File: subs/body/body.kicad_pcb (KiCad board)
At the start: 2 copper layers, 40.8 x 54.8 mm, 80 parts, among them IC1 ATMEGA328P(B), P1 CON_BAT_IN, P3 CON_POLOLU_PWR2, P4 CONN_BREAKOUT4, P5 CONN_BREAKOUT2, P6 CONN_BREAKOUT3, P7 CONN_BREAKOUT5, P8 CON_BAT_OUT, Q1 CSD25402Q3A, Q2 CSD25402Q3A, Q3 CSD25402Q3A, Q4 CSD25402Q3A, Q5 CSD25402Q3A, Q6 CSD25402Q3A, SW1 SPST_Small, SW2 SPST_Small, U1 LTC4412, U10 74LVC2G07, U11 74LVC2G07, U12 LTC4412, U2 LTC4412, U3 DRV8834-SSOP, U4 TMP36GRT, U5 LTC4412, U6 RT9715GGB, 0.7A, U7 RT9715GGB, 0.7A, U8 RT9715GGB, 0.7A, U9 RT9715GGB, 0.7A, Y1 16MHz

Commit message: Before major layout change
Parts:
- removed C13: 100nF, Capacitors_SMD:C_0402
- removed U4: TMP36GRT, TO_SOT_Packages_SMD:SOT-23-5_Handsoldering
- P4: value CONN_BREAKOUT4 -> CONN3
- P5: value CONN_BREAKOUT2 -> CONN1; footprint Socket_Strips:Socket_Strip_Straight_1x12_Pitch1.27mm -> Socket_Strips:Socket_Strip_Straight_1x15_Pitch1.27mm
- P6: value CONN_BREAKOUT3 -> CONN2
- P7: value CONN_BREAKOUT5 -> CONN4
- moved L1 2.05 mm to (65.6, 112.5), turned to 270 degrees
- moved C3 1.63 mm to (64.2, 112.5)
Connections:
- IC1 pad 19: /TMP -> /A6
- P5 pad 11: /A0 -> /SRV_LOCK
- P5 pad 12: /SRV_LOCK -> GND
- P5 pad 6: GND -> /BAT_INT
- P5 pad 7: /BAT_INT -> GND
- P6 pad 13: /LED_CLK -> /LED_DAT
- P6 pad 14: /LED_DAT -> /LED_CLK
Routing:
- net GND: track 64.0 -> 90.8 mm, vias 14 -> 16
- net /A6: track 0.00 -> 12.3 mm
- net /TMP: track 10.4 -> 0.00 mm
- net VCC: track 103.1 -> 96.5 mm
- net /A0: track 12.2 -> 15.1 mm
- net /BAT_STAT2: track 31.0 -> 29.9 mm
- net /BAT_VOLT2: track 40.3 -> 41.2 mm
- net /SRV_LOCK: track 6.09 -> 6.62 mm

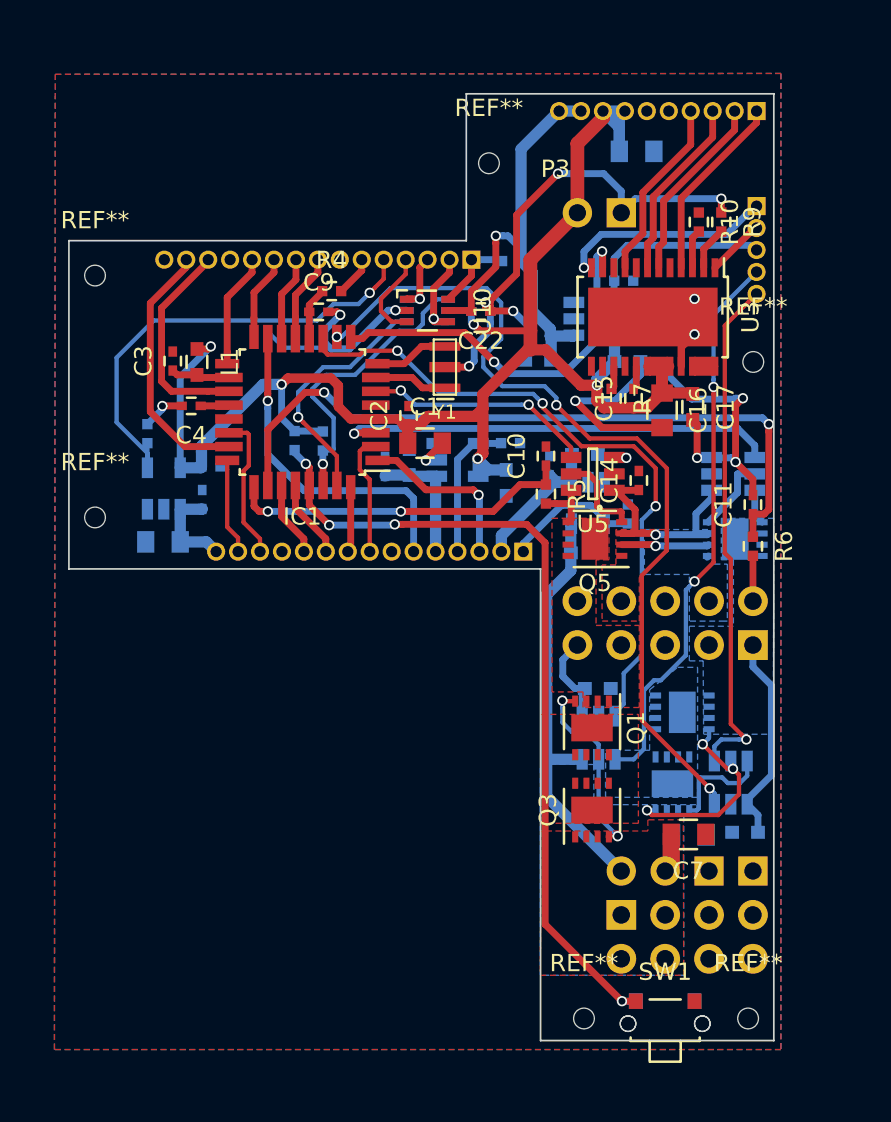
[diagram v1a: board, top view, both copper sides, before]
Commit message: Finished routing of body board
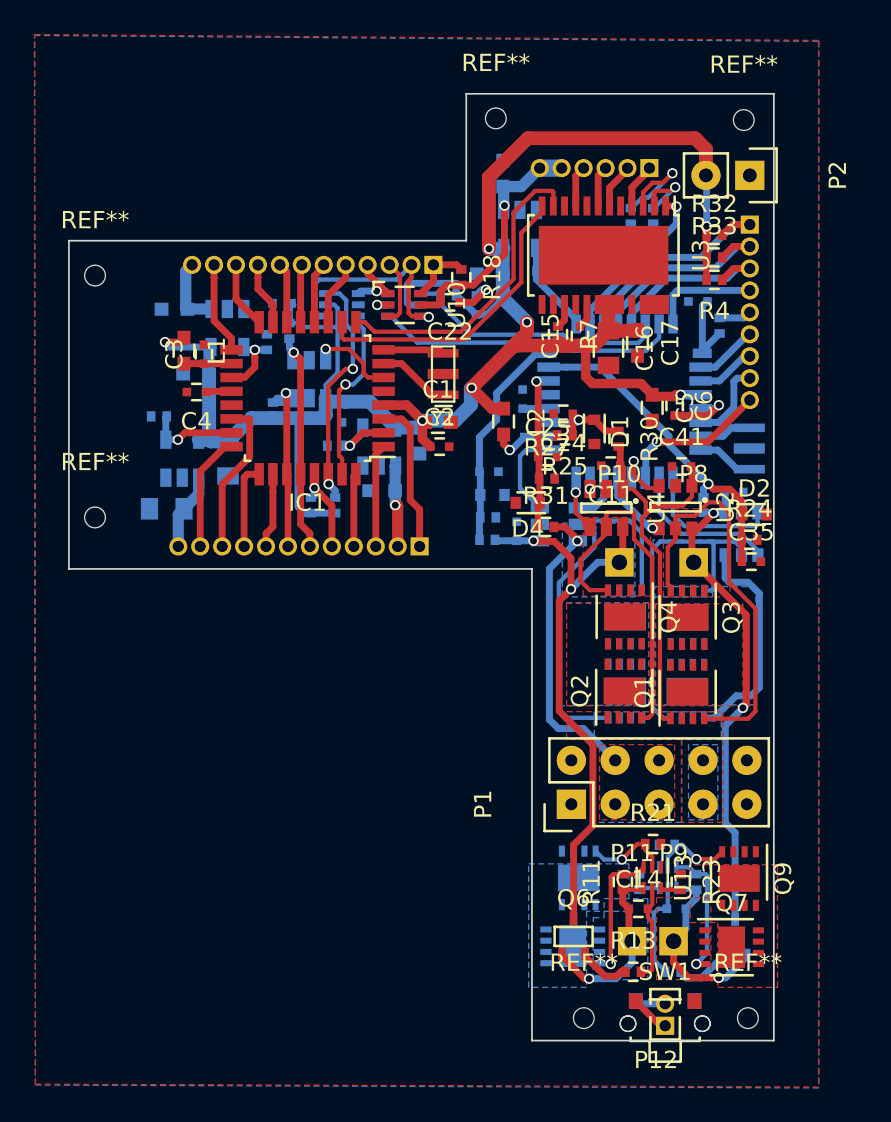
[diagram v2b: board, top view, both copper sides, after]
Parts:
- removed C12: 10uF, Capacitors_SMD:C_0805
- removed C26, C27: 100nF, Capacitors_SMD:C_0402
- removed P3: CON_POLOLU_PWR2, Misc:Pololu-5V-2.54-U3V50F5
- removed the REF** at (82.5, 101.0)
- removed the REF** at (97.8, 112.5)
- added C13: 100nF, Capacitors_SMD:C_0402, B.Cu at (93.4, 144.2)
- added C32: 100nF, Capacitors_SMD:C_0402, B.Cu at (74.0, 115.5)
- added C33: 1uF, Capacitors_SMD:C_0402, B.Cu at (96.7, 120.0)
- added C34: 1uF, Capacitors_SMD:C_0402, B.Cu at (84.1, 122.3)
- added C35: 4.7nF, Capacitors_SMD:C_0402, F.Cu at (97.7, 124.1)
- added C37: 4.7nF, Capacitors_SMD:C_0402, B.Cu at (82.5, 118.9)
- added C41: 100nF, Capacitors_SMD:C_0402, F.Cu at (93.7, 118.6)
- added D1: ESB5B5.0S, Diodes_SMD:SOD-523, F.Cu at (88.6, 116.6)
- added D2: ESB5B5.0S, Diodes_SMD:SOD-523, F.Cu at (97.9, 121.3)
- added D3: ESB5B5.0S, Diodes_SMD:SOD-523, B.Cu at (82.7, 120.2)
- added D4: ESB5B5.0S, Diodes_SMD:SOD-523, F.Cu at (84.8, 120.7)
- added IC2: ATMEGA328P(B), Housings_QFP:TQFP-32_7x7mm_Pitch0.8mm, B.Cu at (90.4, 114.8)
- added L2: 4.7uH, Capacitors_SMD:C_0603, F.Cu at (83.4, 116.0)
- added P10: BAT2+, Pin_Headers:Pin_Header_Straight_1x01, F.Cu at (90.1, 124.1)
- added P11: BAT1-, Pin_Headers:Pin_Header_Straight_1x01, F.Cu at (90.8, 146.1)
- added P12: CONN_RESET, Pin_Headers:Pin_Header_Straight_1x02_Pitch1.27mm, F.Cu at (92.7, 150.9)
- added P2: CONN_VCC, Pin_Headers:Pin_Header_Straight_1x02, F.Cu at (97.6, 101.7)
- added P9: BAT1-, Pin_Headers:Pin_Header_Straight_1x01, F.Cu at (93.2, 146.1)
- added Q10: CSD16327Q3, Housings_DFN_QFN:DFN-8-MOS_3x3mm_Pitch0.65mm, B.Cu at (87.7, 142.4)
- added Q11: CSD25404Q3A, Housings_DFN_QFN:DFN-8-MOS_3x3mm_Pitch0.65mm, B.Cu at (94.0, 127.3)
- added Q12: CSD25404Q3A, Housings_DFN_QFN:DFN-8-MOS_3x3mm_Pitch0.65mm, B.Cu at (90.4, 127.3)
- added Q13: CSD25404Q3A, Housings_DFN_QFN:DFN-8-MOS_3x3mm_Pitch0.65mm, B.Cu at (94.0, 131.6)
- added Q14: CSD25404Q3A, Housings_DFN_QFN:DFN-8-MOS_3x3mm_Pitch0.65mm, B.Cu at (90.4, 131.6)
- added Q7: CSD16327Q3, Housings_DFN_QFN:DFN-8-MOS_3x3mm_Pitch0.65mm, F.Cu at (96.6, 146.4)
- added Q8: CSD16327Q3, Housings_DFN_QFN:DFN-8-MOS_3x3mm_Pitch0.65mm, B.Cu at (87.4, 146.3)
- added Q9: CSD16327Q3, Housings_DFN_QFN:DFN-8-MOS_3x3mm_Pitch0.65mm, F.Cu at (97.0, 142.4)
- added R11: 5M, Resistors_SMD:R_0402, F.Cu at (90.3, 142.6)
- added R12: 330, Resistors_SMD:R_0402, B.Cu at (93.2, 147.8)
- added R13: 330, Resistors_SMD:R_0402, F.Cu at (90.9, 147.8)
- added R2: 10K, Resistors_SMD:R_0402, B.Cu at (71.0, 110.7)
- added R20: 5M, Resistors_SMD:R_0402, B.Cu at (92.8, 140.5)
- added R21: 5M, Resistors_SMD:R_0402, F.Cu at (92.0, 140.4)
- added R22: 2.2K, Resistors_SMD:R_0402, B.Cu at (91.2, 142.6)
- added R23: 2.2K, Resistors_SMD:R_0402, F.Cu at (93.6, 142.6)
- added R24: 1M, Resistors_SMD:R_0402, F.Cu at (97.6, 122.8)
- added R25: 1M, Resistors_SMD:R_0402, F.Cu at (86.9, 116.8)
- added R26: 1M, Resistors_SMD:R_0402, B.Cu at (82.5, 121.5)
- added R27: 1M, Resistors_SMD:R_0402, F.Cu at (85.9, 119.3)
- added R28: 10K, Resistors_SMD:R_0402, B.Cu at (94.9, 120.8)
- added R29: 10K, Resistors_SMD:R_0402, B.Cu at (82.4, 122.8)
- added R3: 10K, Resistors_SMD:R_0402, B.Cu at (70.0, 115.3)
- added R30: 100, Resistors_SMD:R_0402, F.Cu at (90.0, 117.0)
- added R31: 100, Resistors_SMD:R_0402, F.Cu at (85.8, 122.1)
- added R32: 10K, Resistors_SMD:R_0402, F.Cu at (95.6, 105.2)
- added R33: 10K, Resistors_SMD:R_0402, F.Cu at (95.6, 106.5)
- added R8: 5M, Resistors_SMD:R_0402, B.Cu at (94.5, 142.6)
- added REF**: MountingHole_1.2mm_M1, Mounting_Holes:MountingHole_1.2mm_M1, F.Cu at (97.3, 98.5)
- added REF**: MountingHole_1.2mm_M1, Mounting_Holes:MountingHole_1.2mm_M1, F.Cu at (82.9, 98.4)
- added U13: bq29700, Housings_DFN_QFN:DFN-6-1.5x1.5mm_Pitch0.5mm, F.Cu at (92.0, 142.4)
- added U14: LTC4412, TO_SOT_Packages_SMD:SOT-23-6, B.Cu at (97.1, 122.5)
- added U15: LTC4412, TO_SOT_Packages_SMD:SOT-23-6, B.Cu at (86.6, 121.9)
- added U4: LTC4412, TO_SOT_Packages_SMD:SOT-23-6, F.Cu at (89.3, 121.0)
- added Y2: 16MHz, Crystals:Resonator_3x1.3mm, B.Cu at (97.6, 117.5)
- C1: footprint Capacitors_SMD:C_0805 -> Capacitors_SMD:C_0603
- C10, C9: moved to B.Cu
- C18: footprint Capacitors_SMD:C_0402 -> Capacitors_SMD:C_0805
- C24, C25: value 100nF -> 100pF; moved to F.Cu
- C5: value 1uF -> 10uF; moved to F.Cu
- C6: value 1uF -> 100nF; footprint Capacitors_SMD:C_0603 -> Capacitors_SMD:C_0402; moved to F.Cu
- C7: value 22uF -> 100nF; footprint Capacitors_SMD:C_0805 -> Capacitors_SMD:C_0402; moved to B.Cu
- C8: value 22uF -> 100nF; footprint Capacitors_SMD:C_0805 -> Capacitors_SMD:C_0402
- L1: value 10uH -> 4.7uH
- P1: value CON_BAT_IN -> CONN5; moved to F.Cu
- P4: footprint Socket_Strips:Socket_Strip_Straight_1x10_Pitch1.27mm -> Socket_Strips:Socket_Strip_Straight_1x06_Pitch1.27mm
- P5, P6: footprint Socket_Strips:Socket_Strip_Straight_1x15_Pitch1.27mm -> Socket_Strips:Socket_Strip_Straight_1x12_Pitch1.27mm
- P7: footprint Socket_Strips:Socket_Strip_Straight_1x05_Pitch1.27mm -> Socket_Strips:Socket_Strip_Straight_1x09_Pitch1.27mm
- P8: value CON_BAT_OUT -> BAT1+; footprint Pin_Headers:Pin_Header_Straight_2x04 -> Pin_Headers:Pin_Header_Straight_1x01; moved to F.Cu
- Q1, Q3: value CSD25402Q3A -> CSD25404Q3A
- Q2, Q4: value CSD25402Q3A -> CSD25404Q3A; moved to F.Cu
- Q5: value CSD25402Q3A -> MTM231232LBF; footprint Housings_DFN_QFN:DFN-8-MOS_3x3mm_Pitch0.65mm -> TO_SOT_Packages_SMD:SC-70; moved to B.Cu
- Q6: value CSD25402Q3A -> MTM231232LBF; footprint Housings_DFN_QFN:DFN-8-MOS_3x3mm_Pitch0.65mm -> TO_SOT_Packages_SMD:SC-70; moved to F.Cu
- R1, R14, R15, R16, R17, R19, R7: footprint Resistors_SMD:R_0402_Handsoldering -> Resistors_SMD:R_0402
- R10, R9: footprint Resistors_SMD:R_0402_Handsoldering -> Resistors_SMD:R_0402; moved to B.Cu
- R18: footprint Resistors_SMD:R_0402_Handsoldering -> Resistors_SMD:R_0402; moved to F.Cu
- R4: value 1K -> 10K; footprint Resistors_SMD:R_0402_Handsoldering -> Resistors_SMD:R_0402
- R5: value 10K -> 1K; footprint Resistors_SMD:R_0402_Handsoldering -> Resistors_SMD:R_0402; moved to B.Cu
- R6: value 10K -> 100K; footprint Resistors_SMD:R_0402_Handsoldering -> Resistors_SMD:R_0402; moved to B.Cu
- SW1, SW2: value SPST_Small -> SW_PUSH_Small_Horizontal
- U1: value LTC4412 -> 74LVC2G07; footprint TO_SOT_Packages_SMD:SOT-23-6_Handsoldering -> TO_SOT_Packages_SMD:SC-70-6
- U10, U11: footprint TO_SOT_Packages_SMD:SC-70-6_Handsoldering -> TO_SOT_Packages_SMD:SC-70-6
- U12: value LTC4412 -> TMP101; footprint TO_SOT_Packages_SMD:SOT-23-6_Handsoldering -> TO_SOT_Packages_SMD:SOT-23-6
- U2: footprint TO_SOT_Packages_SMD:SOT-23-6_Handsoldering -> TO_SOT_Packages_SMD:SOT-23-6; moved to F.Cu
- U5: value LTC4412 -> bq29700; footprint TO_SOT_Packages_SMD:SOT-23-6_Handsoldering -> Housings_DFN_QFN:DFN-6-1.5x1.5mm_Pitch0.5mm; moved to B.Cu
- U6, U7, U8, U9: footprint TO_SOT_Packages_SMD:SOT-23-5_Handsoldering -> TO_SOT_Packages_SMD:SOT-23-5
- moved U1 29.1 mm to (74.0, 109.2)
- moved C8 27.0 mm to (84.5, 114.7), turned to 90 degrees
- moved C31 25.2 mm to (64.3, 109.5), turned to 0 degrees
- moved U12 25.1 mm to (72.1, 113.5), turned to 270 degrees
- moved C7 25.1 mm to (84.0, 116.9)
- moved C6 25.0 mm to (93.3, 115.1), turned to 270 degrees
- moved Q6 24.8 mm to (87.4, 145.8)
- moved C14 24.8 mm to (91.2, 144.2), turned to 0 degrees
- moved C21 24.7 mm to (65.6, 113.2), turned to 0 degrees
- moved Q5 24.4 mm to (96.8, 145.8)
- moved U5 23.8 mm to (92.9, 142.4), turned to 270 degrees
- moved U9 23.2 mm to (67.4, 110.6)
- moved R17 23.1 mm to (69.7, 111.4)
- moved R6 22.8 mm to (80.2, 108.7), turned to 0 degrees
- moved R4 22.2 mm to (95.6, 107.8), turned to 180 degrees
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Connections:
- net /BAT_PATH1 renamed /CHG1_PATH2
- net /BAT_PATH2 renamed /CHG2_PATH2
- net /INT renamed /FAN_TACHO
- C10 pad 1: /BAT_VOLT1 -> GND
- C10 pad 2: GND -> VCC
- C11 pad 1: /BAT_VOLT2 -> /CHARGE
- C14 pad 1: /CHARGE -> /BAT2-
- C14 pad 2: GND -> Net-(C14-Pad2)
- C21 pad 2: /BAT -> VCC
- C24 pad 1: GND -> /VCHG
- C24 pad 2: /LED_VOUT -> GND
- C25 pad 1: GND -> /VBAT
- C25 pad 2: EP_VCC -> GND
- C5 pad 1: /BAT_VIN1 -> VCC
- C6 pad 1: /BAT_VIN2 -> VCC
- C7 pad 1: GND -> Net-(C7-Pad1)
- C7 pad 2: /BAT -> GND
- C8 pad 1: GND -> Net-(C8-Pad1)
- C8 pad 2: /BAT -> GND
- IC1 pad 10: /BAT_CTL2 -> /STEP_DIR
- IC1 pad 11: /BAT_CTL1 -> /SRV_CAM
- IC1 pad 12: Net-(C9-Pad1) -> /SRV_FOOT
- IC1 pad 13: /SRV_CAM -> /SRV_BRAKE
- IC1 pad 14: /SRV_FOOT -> /SRV_LOCK
- IC1 pad 15: /FAN_PWM -> /STEP_STOP1
- IC1 pad 16: /SRV_BRAKE -> /STEP_STOP2
- IC1 pad 17: /SRV_LOCK -> /FRAME_STOP
- IC1 pad 19: /A6 -> /SRV_EN
- IC1 pad 2: /IR_RX -> /FAN_EN
- IC1 pad 23: /A0 -> /LED_EN
- IC1 pad 25: /BAT_VOLT1 -> /A2
- IC1 pad 26: /BAT_VOLT2 -> /BUTTON
- IC1 pad 27: /SDA -> /SDA0
- IC1 pad 28: /SCL -> /SCL0
- IC1 pad 29: /RESET -> /~RESET0
- IC1 pad 3: /CHG_STAT2 -> /PE0
- IC1 pad 30: /RXD -> /RXD0
- IC1 pad 31: /TXD -> /TXD0
- IC1 pad 32: /IR_TX -> /FAN_PWM
- IC1 pad 6: /CHG_STAT1 -> /TMP_INT0
- P1 pad 1: /BAT_VIN2 -> GND
- P1 pad 10: /BAT_VIN1 -> GND
- P1 pad 2: /BAT_VIN2 -> GND
- P1 pad 3: /BAT_VIN2 -> /BAT
- P1 pad 4: /CHARGE -> /BAT
- P1 pad 5: GND -> /BAT
- P1 pad 6: GND -> /BAT
- P1 pad 7: /BAT_VIN1 -> /CHARGE
- P1 pad 9: /BAT_VIN1 -> GND
- P4 pad 5: GND -> EP_VCC
- P4 pad 6: GND -> EP_VCC
- P5 pad 10: /SRV_BRAKE -> /STEP_STOP2
- P5 pad 11: /SRV_LOCK -> /FRAME_STOP
- P5 pad 12: GND -> /SRV_VOUT
- P5 pad 3: /UART_RX -> /EP_TXD
- P5 pad 4: /EP_TXD -> /UART_RX
- P5 pad 5: /LED_EN -> /SRV_CAM
- P5 pad 6: /BAT_INT -> /SRV_FOOT
- P5 pad 7: GND -> /SRV_BRAKE
- P5 pad 8: /SRV_CAM -> /SRV_LOCK
- P5 pad 9: /SRV_FOOT -> /STEP_STOP1
- P6 pad 1: /SRV_EN -> /PE0
- P6 pad 10: /SCL -> /LED_DAT
- P6 pad 11: /SDA -> /LED_CLK
- P6 pad 12: GND -> /LED_VOUT
- P6 pad 2: /SRV_VOUT -> /FAN_VOUT
- P6 pad 4: /FAN_EN -> /FAN_PWM
- P6 pad 5: /FAN_VOUT -> /~RESET0
- P6 pad 6: /FAN_PWM -> /SCL0
- P6 pad 7: GND -> /SDA0
- P6 pad 8: /IR_RX -> /BUTTON
- P6 pad 9: /IR_TX -> /A2
- P7 pad 1: /STEP_DIR -> /SDA1
- P7 pad 2: /~STEP_SLP -> /SCL1
- P7 pad 3: /EP_EN -> /~RESET1
- P7 pad 4: /BAT_STAT1 -> /IR_TX
- P7 pad 5: /BAT_STAT2 -> /BAT_INT
- P8 pad 1: /BAT -> /BAT1+
- Q1 pad 1: /BAT_VIN1 -> /CHARGE
- Q1 pad 2: /BAT_VIN1 -> /CHARGE
- Q1 pad 3: /BAT_VIN1 -> /CHARGE
- Q2 pad 1: /BAT_VIN2 -> /CHARGE
- Q2 pad 2: /BAT_VIN2 -> /CHARGE
- Q2 pad 3: /BAT_VIN2 -> /CHARGE
- Q3 pad 1: /BAT -> /BAT1+
- Q3 pad 2: /BAT -> /BAT1+
- Q3 pad 3: /BAT -> /BAT1+
- Q4 pad 1: /BAT -> /BAT2+
- Q4 pad 2: /BAT -> /BAT2+
- Q4 pad 3: /BAT -> /BAT2+
- Q5 pad 1: /CHARGE -> /BAT1-
- Q5 pad 2: /CHARGE -> Net-(Q5-Pad2)
- Q5 pad 3: /CHARGE -> /BAT1+
- Q6 pad 1: /CHARGE -> /BAT2-
- Q6 pad 2: /CHARGE -> Net-(Q6-Pad2)
- Q6 pad 3: /CHARGE -> /BAT2+
- R1 pad 1: /RESET -> /~RESET0
- R19 pad 1: /RXD -> /RXD0
- R4 pad 1: Net-(C9-Pad1) -> /~RESET1
- R4 pad 2: /BAT_INT -> VCC
- R5 pad 1: /BAT_VOLT1 -> Net-(C9-Pad1)
- R5 pad 2: /BAT_VIN1 -> /BAT_INT
- R6 pad 1: /BAT_VOLT2 -> /RXD1
- R6 pad 2: /BAT_VIN2 -> VCC
- SW1 pad 1: /RESET -> /~EXT_RST1
- SW2 pad 2: /RESET -> /~EXT_RST2
- U1 pad 1: /BAT_VIN1 -> /UART_RX
- U1 pad 3: /BAT_CTL1 -> /TXD0
- U1 pad 4: /BAT_STAT1 -> /UART_TX
- U1 pad 5: Net-(Q1-Pad4) -> VCC
- U1 pad 6: /BAT -> /RXD0
- U11 pad 1: /TXD -> /TXD1
- U11 pad 4: /RXD -> /RXD1
- U12 pad 1: /CHARGE -> /SCL0
- U12 pad 3: GND -> /TMP_INT0
- U12 pad 4: /CHG_STAT2 -> VCC
- U12 pad 5: Net-(Q6-Pad4) -> (no net)
- U12 pad 6: /BAT_VIN2 -> /SDA0
- U2 pad 1: /BAT_VIN2 -> /CHARGE
- U2 pad 3: /BAT_CTL2 -> /CHG1_CTL
- U2 pad 4: /BAT_STAT2 -> /CHG1_STAT
- U2 pad 5: Net-(Q2-Pad4) -> Net-(Q1-Pad4)
- U2 pad 6: /BAT -> /BAT1+
- U5 pad 1: /CHARGE -> (no net)
- U5 pad 2: GND -> /COUT1
- U5 pad 3: GND -> Net-(Q7-Pad4)
- U5 pad 4: /CHG_STAT1 -> /BAT1-
- U5 pad 5: Net-(Q5-Pad4) -> Net-(C13-Pad2)
- U5 pad 6: /BAT_VIN1 -> Net-(R22-Pad2)
- U9 pad 5: /BAT -> VCC
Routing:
- net GND: track 90.8 -> 7.76 mm, vias 16 -> 3
- net /BAT_CTL2: track 50.3 -> 0.00 mm, vias 3 -> 0
- net /RESET: track 48.1 -> 0.00 mm, vias 4 -> 0
- net /BAT_VOLT2: track 41.2 -> 0.00 mm, vias 2 -> 0
- net /BAT_CTL1: track 37.9 -> 0.00 mm, vias 3 -> 0
- net /BAT2+: track 0.00 -> 33.2 mm, vias 0 -> 2
- net /BAT_STAT1: track 32.5 -> 0.00 mm, vias 2 -> 0
- net /BAT_STAT2: track 29.9 -> 0.00 mm, vias 1 -> 0
- net /BAT1+: track 0.00 -> 28.6 mm, vias 0 -> 2
- net /CHG_STAT2: track 25.7 -> 0.00 mm, vias 1 -> 0
- net VCC: track 96.5 -> 119.8 mm, vias 5 -> 7
- net Net-(Q12-Pad4): track 0.00 -> 23.0 mm
- net /LED_EN: track 27.0 -> 5.34 mm
- net /BAT_VOLT1: track 20.0 -> 0.00 mm, vias 2 -> 0
- net Net-(Q11-Pad4): track 0.00 -> 19.8 mm
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- added copper zone on B.Cu, net /BAT1+
- added copper zone on F.Cu, net /BAT1+
- added copper zone on F.Cu, net /BAT1-
- added copper zone on F.Cu, net /BAT1_PATH
- added copper zone on B.Cu, net /BAT1_PATH2
- added copper zone on B.Cu, net /BAT2+
- added copper zone on F.Cu, net /BAT2+
- added copper zone on B.Cu, net /BAT2-
- added copper zone on B.Cu, net /BAT2_PATH
- added copper zone on B.Cu, net /BAT2_PATH2
- added copper zone on F.Cu, net /CHG2_PATH2
- removed copper zone on F.Cu, net /BAT_VIN1
- removed copper zone on B.Cu, net /BAT_VIN2
- removed copper zone on B.Cu, net /CHG2_PATH2
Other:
- outline, holes or cut-outs redrawn

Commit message: In progress, commit for backup
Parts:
- removed P12: CONN_RESET, Pin_Headers:Pin_Header_Straight_1x02_Pitch1.27mm
- C29, SW2: moved to F.Cu
- C35, D2, SW1: moved to B.Cu
- P4: footprint Socket_Strips:Socket_Strip_Straight_1x06_Pitch1.27mm -> Pin_Headers:Pin_Header_Straight_1x06_Pitch1.27mm
- P5: footprint Socket_Strips:Socket_Strip_Straight_1x12_Pitch1.27mm -> Pin_Headers:Pin_Header_Straight_1x12_Pitch1.27mm
- P6: footprint Socket_Strips:Socket_Strip_Straight_1x12_Pitch1.27mm -> Pin_Headers:Pin_Header_Straight_1x15_Pitch1.27mm
- P7: footprint Socket_Strips:Socket_Strip_Straight_1x09_Pitch1.27mm -> Pin_Headers:Pin_Header_Straight_1x09_Pitch1.27mm
- Q1, Q11, Q12, Q13, Q14, Q2, Q3, Q4: value CSD25404Q3A -> AON7423
- Q10, Q9: value CSD16327Q3 -> CSD16327Q3/AON7524
- Q5, Q6: value MTM231232LBF -> AO3401; footprint TO_SOT_Packages_SMD:SC-70 -> TO_SOT_Packages_SMD:SOT-23
- Q7, Q8: value CSD16327Q3 -> AON7524/CSD16327Q3
- R24: value 1M -> 2M; moved to B.Cu
- R25: value 1M -> 5M; moved to B.Cu
- R26: value 1M -> 2M
- R27: value 1M -> 5M
- U12: value TMP101 -> MCP9808; footprint TO_SOT_Packages_SMD:SOT-23-6 -> Housings_DFN_QFN:DFN-8-1EP_3x2mm_Pitch0.5mm
- moved C35 14.2 mm to (88.3, 113.4), turned to 270 degrees
- moved R24 12.4 mm to (89.6, 113.3), turned to 270 degrees
- moved D2 10.4 mm to (91.0, 113.6), turned to 270 degrees
- moved L2 7.14 mm to (90.4, 115.0)
- moved R25 4.94 mm to (84.5, 112.5), turned to 90 degrees
- moved R2 4.72 mm to (70.8, 115.4), turned to 180 degrees
- moved R26 3.60 mm to (78.9, 120.9), turned to 90 degrees
- moved C28 2.97 mm to (66.8, 120.9), turned to 180 degrees
- moved P2 2.91 mm to (94.7, 101.7), turned to 90 degrees
- moved C37 2.53 mm to (80.2, 117.9), turned to 90 degrees
- moved R29 2.48 mm to (80.5, 121.2)
- moved D1 2.14 mm to (86.9, 115.2), turned to 180 degrees
- moved D3 1.95 mm to (80.8, 119.8)
- moved D4 1.94 mm to (85.3, 118.8), turned to 0 degrees
- moved P6 1.90 mm to (80.4, 123.2)
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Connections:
- IC1 pad 15: /STEP_STOP1 -> /MOSI0
- IC1 pad 16: /STEP_STOP2 -> /MISO0
- IC1 pad 3: /PE0 -> /TMP_INT0
- IC1 pad 6: /TMP_INT0 -> /TMP_ADDR
- IC2 pad 11: /TMP_INT1 -> /HOST_INT
- IC2 pad 19: /VCHG -> /VBAT2
- IC2 pad 23: /VBAT1 -> /VCHG
- IC2 pad 24: /VBAT2 -> /VBAT1
- IC2 pad 6: /HOST_INT -> /TMP_INT1
- P5 pad 10: /STEP_STOP2 -> /MOSI0
- P5 pad 11: /FRAME_STOP -> /MISO0
- P5 pad 12: /SRV_VOUT -> /FRAME_STOP
- P5 pad 9: /STEP_STOP1 -> /SRV_VOUT
- P6 pad 1: /PE0 -> /CHG2_STAT
- P6 pad 10: /LED_DAT -> /SDA0
- P6 pad 11: /LED_CLK -> /BUTTON
- P6 pad 12: /LED_VOUT -> /A2
- P6 pad 2: /FAN_VOUT -> /CHG2_CTL
- P6 pad 3: /FAN_TACHO -> /BAT2_CTL
- P6 pad 4: /FAN_PWM -> /TMP_INT0
- P6 pad 5: /~RESET0 -> /FAN_VOUT
- P6 pad 6: /SCL0 -> /FAN_TACHO
- P6 pad 7: /SDA0 -> /FAN_PWM
- P6 pad 8: /BUTTON -> /~RESET0
- P6 pad 9: /A2 -> /SCL0
- Q1 pad 1: /CHARGE -> /CHG1_PATH2
- Q1 pad 2: /CHARGE -> /CHG1_PATH2
- Q1 pad 3: /CHARGE -> /CHG1_PATH2
- Q1 pad 5: /CHG1_PATH2 -> /CHARGE
- Q1 pad 6: /CHG1_PATH2 -> /CHARGE
- Q1 pad 7: /CHG1_PATH2 -> /CHARGE
- Q1 pad 8: /CHG1_PATH2 -> /CHARGE
- Q11 pad 1: /BAT1+ -> /BAT1_PATH2
- Q11 pad 2: /BAT1+ -> /BAT1_PATH2
- Q11 pad 3: /BAT1+ -> /BAT1_PATH2
- Q11 pad 5: /BAT1_PATH2 -> /BAT1+
- Q11 pad 6: /BAT1_PATH2 -> /BAT1+
- Q11 pad 7: /BAT1_PATH2 -> /BAT1+
- Q11 pad 8: /BAT1_PATH2 -> /BAT1+
- Q12 pad 1: /BAT2+ -> /BAT2_PATH2
- Q12 pad 2: /BAT2+ -> /BAT2_PATH2
- Q12 pad 3: /BAT2+ -> /BAT2_PATH2
- Q12 pad 5: /BAT2_PATH2 -> /BAT2+
- Q12 pad 6: /BAT2_PATH2 -> /BAT2+
- Q12 pad 7: /BAT2_PATH2 -> /BAT2+
- Q12 pad 8: /BAT2_PATH2 -> /BAT2+
- Q13 pad 1: /BAT -> /BAT1_PATH2
- Q13 pad 2: /BAT -> /BAT1_PATH2
- Q13 pad 3: /BAT -> /BAT1_PATH2
- Q13 pad 5: /BAT1_PATH2 -> /BAT
- Q13 pad 6: /BAT1_PATH2 -> /BAT
- Q13 pad 7: /BAT1_PATH2 -> /BAT
- Q13 pad 8: /BAT1_PATH2 -> /BAT
- Q14 pad 1: /BAT -> /BAT2_PATH2
- Q14 pad 2: /BAT -> /BAT2_PATH2
- Q14 pad 3: /BAT -> /BAT2_PATH2
- Q14 pad 5: /BAT2_PATH2 -> /BAT
- Q14 pad 6: /BAT2_PATH2 -> /BAT
- Q14 pad 7: /BAT2_PATH2 -> /BAT
- Q14 pad 8: /BAT2_PATH2 -> /BAT
- Q2 pad 1: /CHARGE -> /CHG2_PATH2
- Q2 pad 2: /CHARGE -> /CHG2_PATH2
- Q2 pad 3: /CHARGE -> /CHG2_PATH2
- Q2 pad 5: /CHG2_PATH2 -> /CHARGE
- Q2 pad 6: /CHG2_PATH2 -> /CHARGE
- Q2 pad 7: /CHG2_PATH2 -> /CHARGE
- Q2 pad 8: /CHG2_PATH2 -> /CHARGE
- Q3 pad 1: /BAT1+ -> /CHG1_PATH2
- Q3 pad 2: /BAT1+ -> /CHG1_PATH2
- Q3 pad 3: /BAT1+ -> /CHG1_PATH2
- Q3 pad 5: /CHG1_PATH2 -> /BAT1+
- Q3 pad 6: /CHG1_PATH2 -> /BAT1+
- Q3 pad 7: /CHG1_PATH2 -> /BAT1+
- Q3 pad 8: /CHG1_PATH2 -> /BAT1+
- Q4 pad 1: /BAT2+ -> /CHG2_PATH2
- Q4 pad 2: /BAT2+ -> /CHG2_PATH2
- Q4 pad 3: /BAT2+ -> /CHG2_PATH2
- Q4 pad 5: /CHG2_PATH2 -> /BAT2+
- Q4 pad 6: /CHG2_PATH2 -> /BAT2+
- Q4 pad 7: /CHG2_PATH2 -> /BAT2+
- Q4 pad 8: /CHG2_PATH2 -> /BAT2+
- SW1 pad 1: /~EXT_RST1 -> GND
- SW1 pad 2: GND -> /~RESET0
- SW2 pad 2: /~EXT_RST2 -> /~RESET1
- U12 pad 2: GND -> /SDA0
- U12 pad 4: VCC -> GND
- U12 pad 5: (no net) -> /TMP_ADDR
- U12 pad 6: /SDA0 -> GND
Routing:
- net /~RESET1: track 10.5 -> 57.3 mm
- net /~RESET0: track 5.27 -> 50.1 mm
- net /CHG2_CTL: track 0.65 -> 17.7 mm
- net /TMP_INT0: track 5.00 -> 20.4 mm
- net /CHG2_STAT: track 3.69 -> 14.2 mm
- net /PE0: track 8.86 -> 0.00 mm
- net /CHARGE: track 22.6 -> 31.5 mm
- net /BAT2_CTL: track 5.27 -> 13.9 mm, vias 0 -> 1
- net /TMP_ADDR: track 0.00 -> 5.99 mm, vias 0 -> 1
- net /TMP_INT1: track 8.73 -> 3.38 mm, vias 1 -> 0
- net /MISO0: track 0.00 -> 4.78 mm
- net Net-(Q11-Pad4): track 19.8 -> 24.6 mm
- net /HOST_INT: track 4.79 -> 9.41 mm, vias 0 -> 1
- net /MOSI0: track 0.00 -> 4.21 mm
- net /STEP_STOP2: track 3.88 -> 0.00 mm
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- added copper zone on B.Cu, net /BAT1-
- added copper zone on F.Cu, net /BAT2-

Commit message: Major modification of body board and companions
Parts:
- removed C32: 100nF, Capacitors_SMD:C_0402
- removed U12: MCP9808, Housings_DFN_QFN:DFN-8-1EP_3x2mm_Pitch0.5mm
- P5: footprint Pin_Headers:Pin_Header_Straight_1x12_Pitch1.27mm -> Pin_Headers:Pin_Header_Straight_1x13_Pitch1.27mm
- Q5, Q6: value AO3401 -> AO3419/AO3401
- moved R2 4.89 mm to (69.5, 120.1), turned to 270 degrees
- moved R3 3.90 mm to (70.8, 120.1), turned to 270 degrees
- moved C9 3.45 mm to (93.2, 112.2), turned to 270 degrees
- moved R17 2.97 mm to (68.0, 113.0), turned to 0 degrees
- moved C10 1.87 mm to (72.5, 111.0), turned to 0 degrees
- moved R15 1.84 mm to (86.6, 105.7), turned to 270 degrees
- moved R28 1.62 mm to (95.0, 119.2)
- moved REF** 1.50 mm to (86.5, 150.5)
- moved SW1 1.21 mm to (91.5, 150.8)
- moved SW2 1.21 mm to (91.5, 150.8)
- moved R16 1.20 mm to (73.5, 116.4)
- moved R18 1.08 mm to (80.1, 108.3), turned to 0 degrees
- moved C19 1.00 mm to (83.3, 108.1), turned to 90 degrees
- moved C29 1.00 mm to (82.7, 102.3), turned to 0 degrees
- moved REF** 1.00 mm to (83.5, 98.3)
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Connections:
- net /TMP_INT1 renamed /SCL2
- IC1 pad 1: /FAN_TACHO -> /FAN_PWM
- IC1 pad 10: /STEP_DIR -> /STEP
- IC1 pad 2: /FAN_EN -> /HOST_INT
- IC1 pad 3: /TMP_INT0 -> /FAN_EN
- IC1 pad 32: /FAN_PWM -> /FAN_TACHO
- IC1 pad 6: /TMP_ADDR -> /~STEP_SLP
- IC1 pad 9: /STEP -> /STEP_DIR
- IC2 pad 1: Net-(C9-Pad1) -> /IR_TX
- IC2 pad 11: /HOST_INT -> /CHG1_CTL
- IC2 pad 12: /CHG1_CTL -> /CHG1_STAT
- IC2 pad 13: /CHG1_STAT -> /BAT2_STAT
- IC2 pad 14: /BAT2_STAT -> /BAT2_CTL
- IC2 pad 17: /BAT2_CTL -> /TMP_INT
- IC2 pad 26: /~STEP_SLP -> /PWR_INT
- IC2 pad 3: /PWR_INT -> /SDA2
- IC2 pad 32: /IR_TX -> Net-(C9-Pad1)
- P5 pad 9: /SRV_VOUT -> /A2
- P6 pad 10: /SDA0 -> /SCL0
- P6 pad 11: /BUTTON -> /SDA0
- P6 pad 12: /A2 -> /BUTTON
- P6 pad 4: /TMP_INT0 -> /FAN_VOUT
- P6 pad 5: /FAN_VOUT -> /TMP_INT
- P6 pad 6: /FAN_TACHO -> /FAN_PWM
- P6 pad 7: /FAN_PWM -> /HOST_INT
- P6 pad 8: /~RESET0 -> /FAN_TACHO
- P6 pad 9: /SCL0 -> /~RESET0
- P7 pad 1: /SDA1 -> /PWR_INT
- P7 pad 2: /SCL1 -> /SDA1
- P7 pad 3: /~RESET1 -> /SCL1
- P7 pad 4: /IR_TX -> /~RESET1
- P7 pad 6: /IR_RX -> /IR_TX
- P7 pad 7: /PWR_INT -> /IR_RX
- P7 pad 8: /HOST_INT -> /SDA2
- R2 pad 2: /SCL0 -> /SDA0
- R3 pad 2: /SDA0 -> /SCL0
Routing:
- net /TMP_INT0: track 20.4 -> 0.00 mm, vias 1 -> 0
- net /~STEP_SLP: track 8.89 -> 24.0 mm, vias 1 -> 2
- net /TMP_INT: track 0.00 -> 12.9 mm, vias 0 -> 1
- net /PWR_INT: track 3.44 -> 12.4 mm
- net /A2: track 5.33 -> 13.4 mm, vias 0 -> 1
- net /TMP_ADDR: track 5.99 -> 0.00 mm, vias 1 -> 0
- net /SDA0: track 12.6 -> 8.95 mm, vias 1 -> 0
- net /EP_EN: track 5.45 -> 9.03 mm
- net /RXD0: track 13.3 -> 16.7 mm
- net /BAT2_CTL: track 13.9 -> 16.9 mm
- net /IR_TX: track 6.24 -> 3.29 mm
- net /~RESET0: track 50.1 -> 53.0 mm, vias 1 -> 0
- net /SDA2: track 0.00 -> 2.89 mm
- net Net-(Q11-Pad4): track 24.6 -> 27.3 mm
- net /STEP: track 17.9 -> 20.3 mm
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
